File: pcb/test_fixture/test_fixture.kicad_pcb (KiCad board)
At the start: 2 copper layers, 71.5 x 74.9 mm, 80 parts, among them J1 UART, J3 Conn_ARM_JTAG_SWD_10, J5 GND, J6 GND, P3.3V1 , U1 SC0915, U2 MIC29302WU, U3 INA186A5IDCKR, U4 INA186A5IDCKR

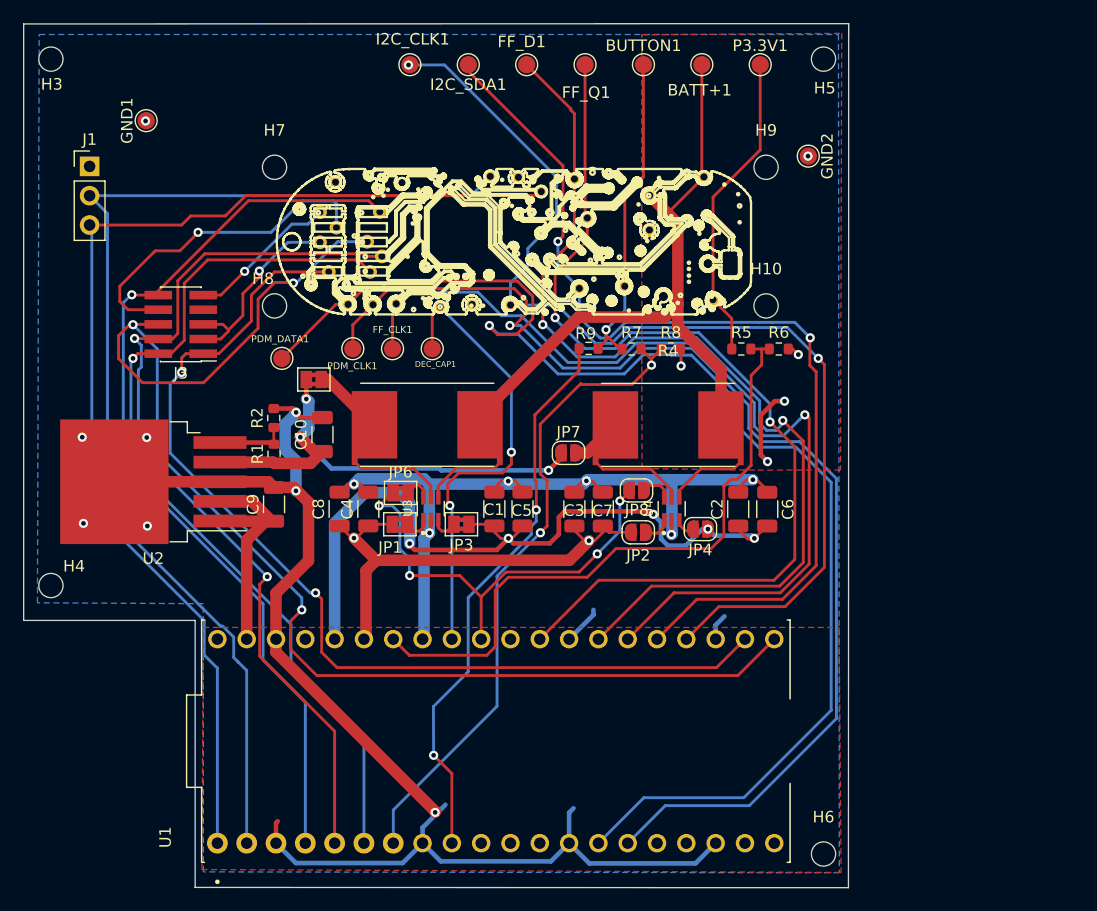
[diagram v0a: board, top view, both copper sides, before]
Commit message: [pcb] updated silkscreen with PCB names
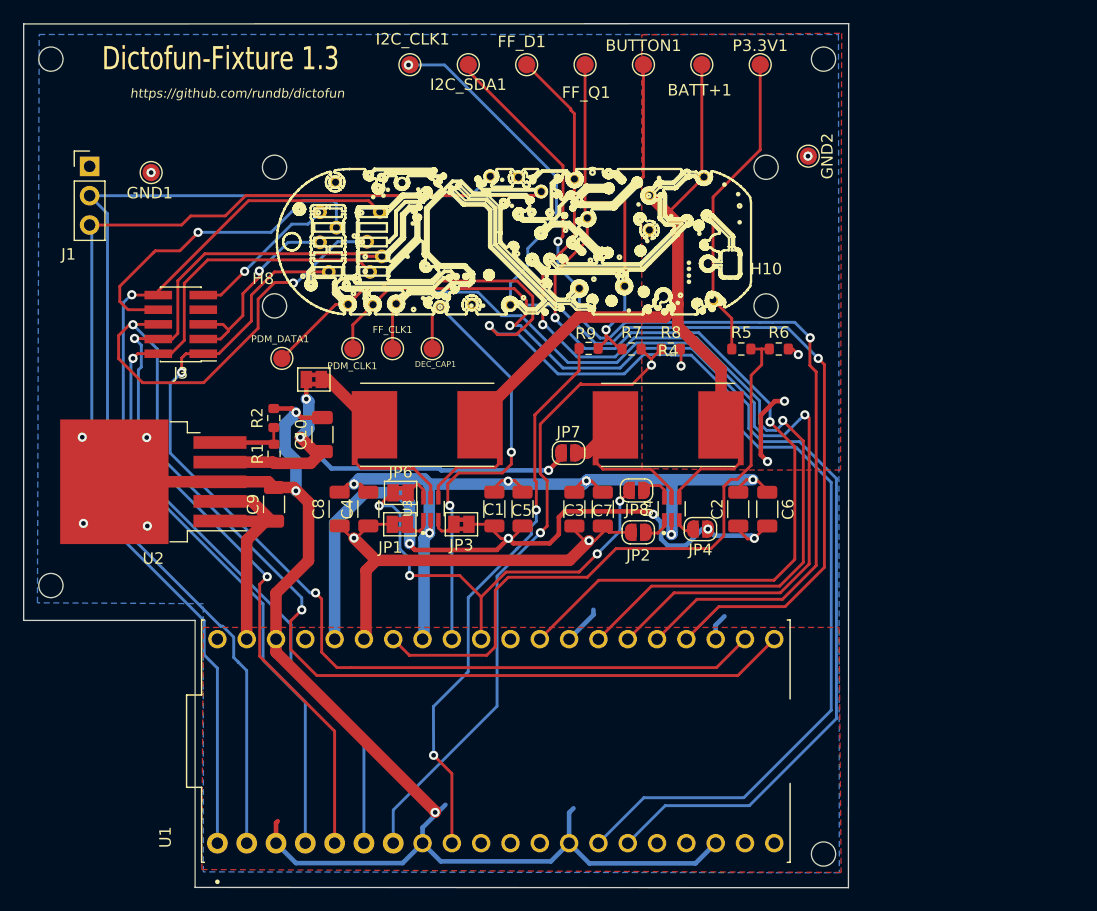
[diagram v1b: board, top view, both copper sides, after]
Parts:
- moved GND1 4.52 mm to (92.8, 81.3)
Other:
- board text added: "Dictofun-Fixture 1.3"
- board text added: "https://github.com/rundb/dictofun"
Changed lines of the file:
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@@
       (drillshape 0)
       (scaleselection 1)
-      (outputdirectory "../out/v1.3_fixture/placement/")
+      (outputdirectory "../out/v1.3_fixture/gerber")
     )
   )
@@
   )
   (footprint "TestPoint:TestPoint_Pad_D1.5mm" (layer "F.Cu")
-    (at 92.3798 76.7588 90)
+    (at 92.8116 81.2546 90)
     (descr "SMD pad as test Point, diameter 1.5mm")
     (tags "test point SMD pad")
@@
     (property "Sheetname" "")
     (attr exclude_from_pos_files)
-    (fp_text reference "GND1" (at 0 -1.648 90) (layer "F.SilkS")
+    (fp_text reference "GND1" (at -1.778 -0.127 180) (layer "F.SilkS")
       (effects (font (size 1 1) (thickness 0.15)))
     )
@@
     (property "Sheetname" "")
     (attr exclude_from_pos_files)
-    (fp_text reference "H9" (at 0 -3.2) (layer "F.SilkS")
+    (fp_text reference "H9" (at 0 -3.2) (layer "F.SilkS") hide
       (effects (font (size 1 1) (thickness 0.15)))
     )
@@
     (property "Sheetname" "")
     (attr exclude_from_pos_files)
-    (fp_text reference "H4" (at 2.0066 -1.6764) (layer "F.SilkS")
+    (fp_text reference "H4" (at 2.0066 -1.6764) (layer "F.SilkS") hide
       (effects (font (size 1 1) (thickness 0.15)))
     )
@@
     (property "Sheetname" "")
     (attr through_hole)
-    (fp_text reference "J1" (at 0 -2.33) (layer "F.SilkS")
+    (fp_text reference "J1" (at -1.8288 7.62) (layer "F.SilkS")
       (effects (font (size 1 1) (thickness 0.15)))
     )
@@
     (property "Sheetname" "")
     (attr exclude_from_pos_files)
-    (fp_text reference "H7" (at 0 -3.2) (layer "F.SilkS")
+    (fp_text reference "H7" (at 0 -3.2) (layer "F.SilkS") hide
       (effects (font (size 1 1) (thickness 0.15)))
     )
@@
     (property "Sheetname" "")
     (attr exclude_from_pos_files)
-    (fp_text reference "H3" (at 0.0762 2.1844) (layer "F.SilkS")
+    (fp_text reference "H3" (at 0.0762 2.1844) (layer "F.SilkS") hide
       (effects (font (size 1 1) (thickness 0.15)))
     )
@@
     (property "Sheetname" "")
     (attr exclude_from_pos_files)
-    (fp_text reference "H6" (at 0 -3.2) (layer "F.SilkS")
+    (fp_text reference "H6" (at 0 -3.2) (layer "F.SilkS") hide
       (effects (font (size 1 1) (thickness 0.15)))
     )
@@
     (property "Sheetname" "")
     (attr exclude_from_pos_files)
-    (fp_text reference "H5" (at 0.1016 2.5146) (layer "F.SilkS")
+    (fp_text reference "H5" (at 0.1016 2.5146) (layer "F.SilkS") hide
       (effects (font (size 1 1) (thickness 0.15)))
     )
@@
   (gr_line (start 153.2382 143.2306) (end 153.2636 68.3514) (layer "Edge.Cuts") (width 0.1))
   (gr_line (start 153.2636 68.3514) (end 81.7626 68.3768) (layer "Edge.Cuts") (width 0.1))
+  (gr_text "Dictofun-Fixture 1.3" (at 98.8314 71.374) (layer "F.Cu")
+    (effects (font (size 2 1.5) (thickness 0.3)))
+  )
+  (gr_text "Dictofun-Fixture 1.3" (at 98.8314 71.374) (layer "F.SilkS")
+    (effects (font (size 2 1.5) (thickness 0.3)))
+  )
+  (gr_text "https://github.com/rundb/dictofun" (at 100.2792 74.3966) (layer "F.SilkS")
+    (effects (font (size 0.8 0.8) (thickness 0.1) italic))
+  )
+  (gr_text "Dictofun-Fixture 1.3" (at 98.8314 71.374) (layer "F.Mask")
+    (effects (font (size 2 1.5) (thickness 0.3)))
+  )
   (segment (start 120.523 83.2612) (end 122.1994 81.5848) (width 0.25) (layer "B.Cu") (net 1))
   (segment (start 89.027 110.7694) (end 89.027 84.8106) (width 0.25) (layer "B.Cu") (net 1))
@@
   (via (at 146.2278 106.299) (size 0.8) (drill 0.4) (layers "F.Cu" "B.Cu") (free) (net 13))
   (via (at 92.4306 104.2162) (size 0.8) (drill 0.4) (layers "F.Cu" "B.Cu") (net 13))
-  (via (at 92.329 76.7842) (size 0.8) (drill 0.4) (layers "F.Cu" "B.Cu") (net 13))
+  (via (at 92.8116 81.2546) (size 0.8) (drill 0.4) (layers "F.Cu" "B.Cu") (net 13))
   (via (at 105.3719 102.0445) (size 0.8) (drill 0.4) (layers "F.Cu" "B.Cu") (net 13))
   (via (at 148.8948 97.028) (size 0.8) (drill 0.4) (layers "F.Cu" "B.Cu") (net 13))

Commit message: fixed another issue (added current limiting resistor, added testpoint for button control)
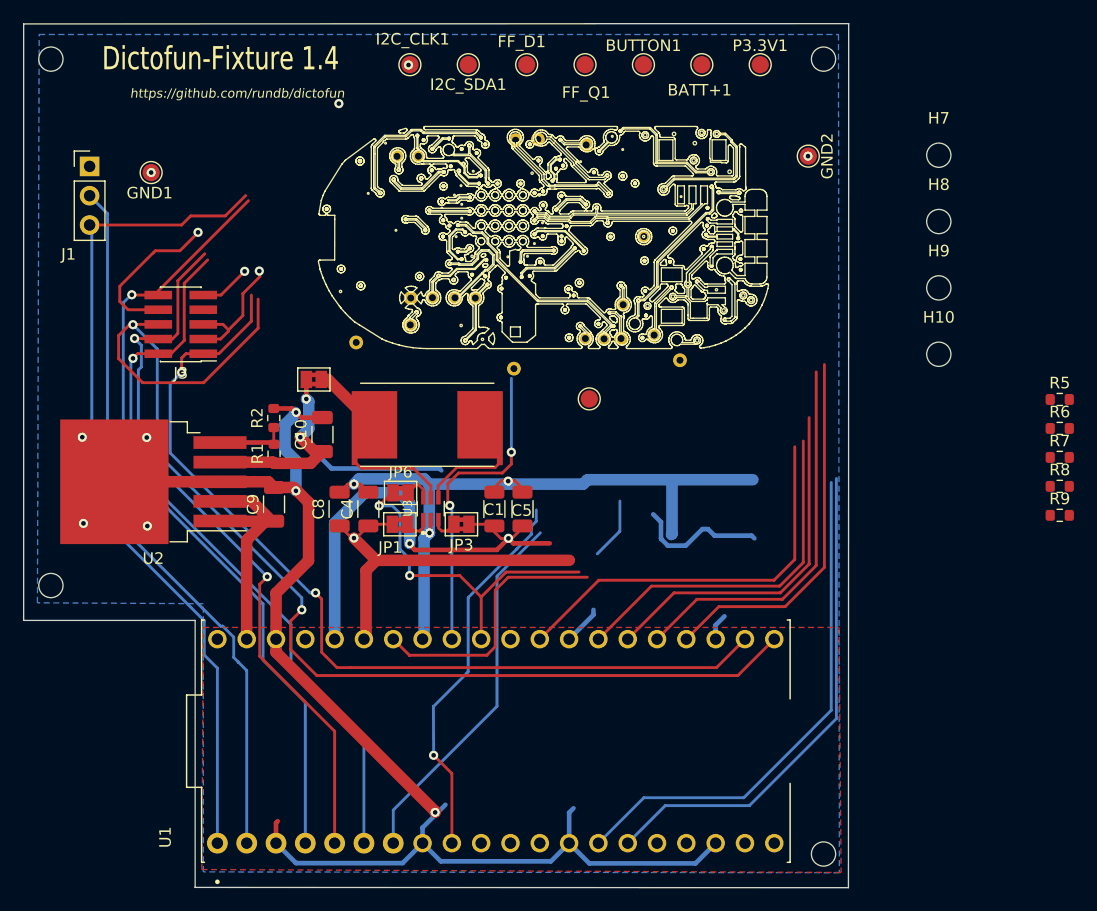
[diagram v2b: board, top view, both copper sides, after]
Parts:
- removed C2, C3: 1u, Resistor_SMD:R_1206_3216Metric
- removed C6, C7: 100n, Resistor_SMD:R_1206_3216Metric
- removed DEC_CAP1, PDM_CLK1, PDM_DATA1: , TestPoint:TestPoint_Pad_D1.5mm
- removed J5, J6: GND, fixture:POGO
- removed JP2, JP4, JP7, JP8: Jumper_2_Open, Jumper:SolderJumper-2_P1.3mm_Open_RoundedPad1.0x1.5mm
- removed POGO17, POGO18, POGO24, POGO25, POGO6: pogo, fixture:POGO
- removed R4: 0.01, Resistor_SMD:R_Shunt_Vishay_WSR2_WSR3_KelvinConnection
- removed U4: INA186A5IDCKR, fixture:SOT65P210X110-6N
- moved H8 58.0 mm to (161.1, 85.5)
- moved H7 57.6 mm to (161.1, 79.8)
- moved R9 43.3 mm to (171.6, 111.0), turned to 0 degrees
- moved R7 38.3 mm to (171.6, 105.9)
- moved R8 35.7 mm to (171.6, 108.5)
- moved POGO16 31.1 mm to (110.6, 96.0)
- moved R5 27.9 mm to (171.6, 100.9)
- moved POGO3 26.8 mm to (133.7, 92.7)
- moved R6 25.3 mm to (171.6, 103.4)
- moved POGO4 23.8 mm to (130.5, 78.9)
- moved POGO10 18.3 mm to (132.1, 95.7)
- moved H9 18.3 mm to (161.1, 91.2)
- moved POGO12 18.0 mm to (116.0, 79.8)
- moved FF_CLK1 17.6 mm to (130.8, 100.9)
- moved POGO23 16.8 mm to (124.2, 98.2)
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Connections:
- P3.3V1 pad 1: /P3.3V -> /P1.9V
- POGO16 pad 1: /P3.3V -> /P1.9V
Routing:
- net /PDM_DATA: track 114.3 -> 44.7 mm, vias 1 -> 0
- net /BATT+: track 72.9 -> 8.07 mm
- net /I2C_CLK: track 92.3 -> 32.1 mm, vias 2 -> 1
- net /PDM_CLK: track 101.6 -> 43.4 mm, vias 1 -> 0
- net /FF_D: track 86.6 -> 31.0 mm, vias 2 -> 0
- net /I2C_DATA: track 84.9 -> 33.8 mm, vias 2 -> 0
- net /FF_Q: track 85.5 -> 34.7 mm, vias 2 -> 0
- net /FF_CLK: track 79.5 -> 31.1 mm, vias 1 -> 0
- net /UART_TX: track 97.4 -> 62.0 mm
- net /SENSE_3_3V: track 55.8 -> 23.1 mm
- net /BUTTON: track 28.3 -> 0.00 mm, vias 1 -> 0
- net /P3.3V: track 27.0 -> 0.00 mm
- net /UART_RX: track 98.5 -> 72.7 mm
- net /BUTTON_DIVIDED: track 57.4 -> 32.2 mm, vias 2 -> 0
- net GND: track 161.0 -> 136.6 mm, vias 15 -> 12
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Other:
- board text added: "Dictofun-Fixture 1.4"
- board text removed: "Dictofun-Fixture 1.3"

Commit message: fixing the state of harness for 1.4.52840
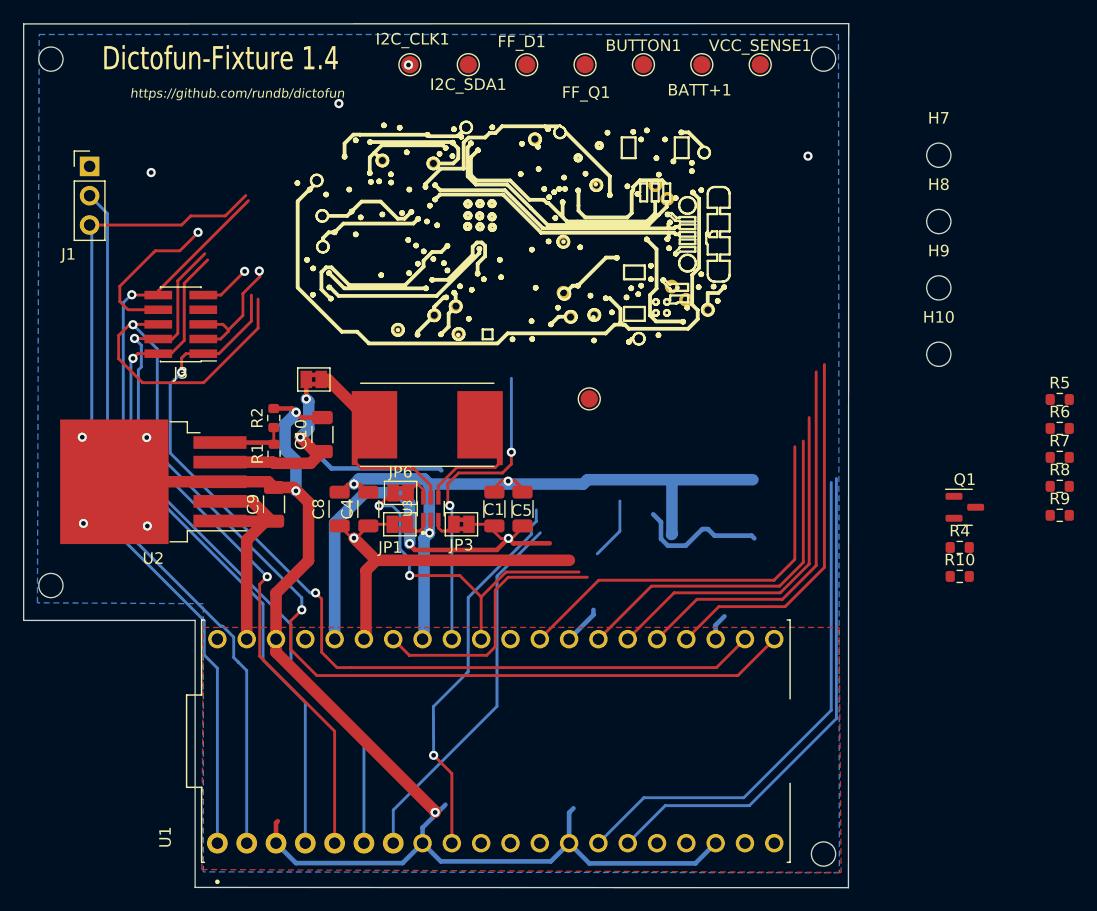
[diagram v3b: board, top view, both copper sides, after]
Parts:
- removed GND1, GND2: , TestPoint:TestPoint_Pad_D1.5mm
- removed POGO20, POGO23, POGO4: pogo, fixture:POGO
- added POGO6: pogo, fixture:POGO, F.Cu at (139.2, 92.3)
- added Q1: NMOS, Package_TO_SOT_SMD:SOT-23, F.Cu at (163.3, 110.3)
- added R10: 1K, Resistor_SMD:R_0603_1608Metric, F.Cu at (162.9, 116.3)
- added R4: 100K, Resistor_SMD:R_0603_1608Metric, F.Cu at (162.9, 113.7)
- moved POGO16 23.5 mm to (126.1, 78.4)
- moved POGO1 12.7 mm to (136.5, 82.3)
- moved POGO5 12.3 mm to (137.5, 83.5)
- moved POGO3 10.6 mm to (131.4, 82.3)
- moved POGO10 9.10 mm to (128.5, 87.3)
- moved POGO7 8.49 mm to (128.5, 91.7)
- moved POGO13 4.99 mm to (141.1, 93.2)
- moved POGO19 4.47 mm to (137.9, 91.1)
- moved POGO14 4.26 mm to (119.5, 95.2)
- moved POGO11 3.21 mm to (117.3, 80.5)
- moved POGO12 3.14 mm to (112.9, 80.2)
- moved POGO15 3.09 mm to (131.2, 93.6)
- moved POGO2 2.96 mm to (114.2, 94.9)
- moved POGO22 2.35 mm to (117.3, 93.6)
- moved POGO8 2.26 mm to (129.2, 93.8)
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- renumbered P3.3V1 to VCC_SENSE1
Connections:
- net /P3.3V renamed /VCC_SENSE
- J3 pad 10: /RESET -> unconnected-(J3-~{RESET}-Pad10)
- J3 pad 6: /SWO -> unconnected-(J3-SWO/TDO-Pad6)
- J3 pad 8: Net-(J3-NC/TDI) -> unconnected-(J3-NC/TDI-Pad8)
- J3 pad 9: GND -> unconnected-(J3-GNDDetect-Pad9)
- R5 pad 2: /SENSE_3_3V -> /SENSE_VCC
- R6 pad 1: /SENSE_3_3V -> /SENSE_VCC
- R9 pad 1: /BUTTON -> /BUTTON_CTRL
- U1 pad 32: /DEC_CAP -> unconnected-(U1-GP27-Pad32)
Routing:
- net unconnected-(U1-GP27-Pad32): track 0.00 -> 27.4 mm, vias 0 -> 2
- net /DEC_CAP: track 27.4 -> 0.00 mm, vias 2 -> 0
- net unconnected-(J3-NC/TDI-Pad8): track 0.00 -> 13.9 mm, vias 0 -> 1
- net Net-(J3-NC/TDI): track 13.9 -> 0.00 mm, vias 1 -> 0
- net unconnected-(J3-GNDDetect-Pad9): track 0.00 -> 4.44 mm, vias 0 -> 1
- net GND: track 136.6 -> 132.2 mm, vias 12 -> 11
